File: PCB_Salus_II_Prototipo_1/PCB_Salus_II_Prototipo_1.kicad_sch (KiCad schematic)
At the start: 52 parts, among them J1 Servo1, J10 Conn_01x07_Pin, J11 Conector Entrada 5V, J12 Conector 5V, J13 Conector Entrada 7V, J14 Conector Salida 7V, J15 Sensor 1, J16 Luz2, J17 Cambios1, J18 Cambios 2, J19 MarchaAtras1, J2 Sensor Giro, J20 MarchaAtras2, J21 Sobrante1, J22 Sobrante2, J23 Arranque1, J24 Arranque2, J25 ControlMotor, J26 Sensor 2, J27 Sensor 3, J28 Sensor 4, J29 Sensor 5, J3 Acelerador, J30 Sensor 6, J31 Sensor 7, J4 Conn_01x05_Pin, J5 Servo2, J6 Antena, J7 SensorGiro, J8 Luz1, J9 Conn_01x07_Pin, K1 Rele 5V, K2 Rele 7V, K3 Arranque, Q1 IO25, Q2 IO26, Q3 IO27, Q4 IO14, U1 ESP32-DEVKITC-32D, U2 RASPBERRY_PI_4B_4GB

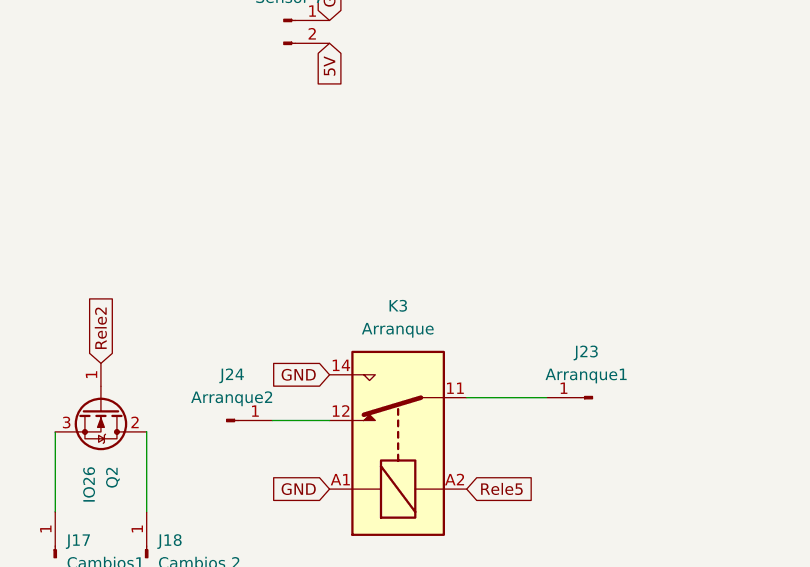
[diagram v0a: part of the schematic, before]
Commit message: se agrego mensaje para modificar conexion Rele
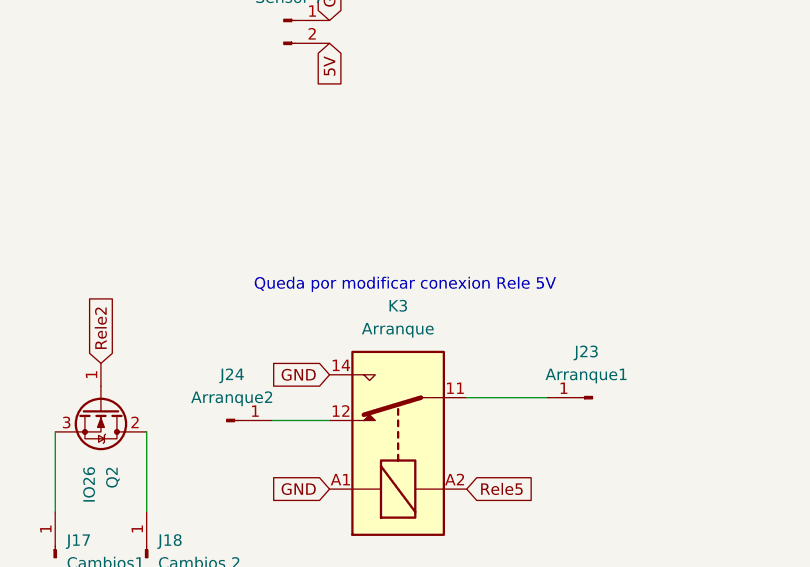
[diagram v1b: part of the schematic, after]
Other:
- note added: "Queda por modificar conexion Rele 5V"
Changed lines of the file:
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@@
+		)
+	)
+	(text "Queda por modificar conexion Rele 5V\n\n"
+		(exclude_from_sim no)
+		(at 149.352 154.94 0)
+		(effects
+			(font
+				(size 1.27 1.27)
+			)
 		)
 	)
